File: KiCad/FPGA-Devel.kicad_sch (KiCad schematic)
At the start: 4 parts

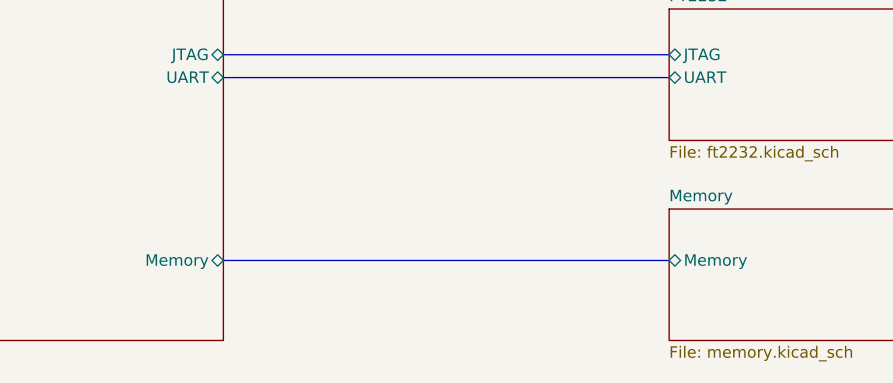
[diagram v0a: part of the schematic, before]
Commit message: micro-SD hinzugefügt
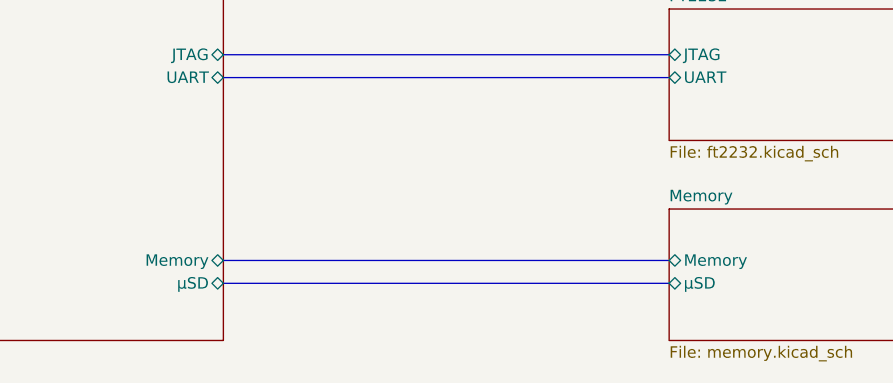
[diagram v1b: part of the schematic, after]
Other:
- sheet FPGA ports: added μSD; removed none
- sheet Memory ports: added μSD; removed none
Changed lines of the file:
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@@
+	(bus
+		(pts
+			(xy 152.4 152.4) (xy 201.93 152.4)
+		)
+		(stroke
+			(width 0)
+			(type default)
+		)
+	)
 	(bus
 		(pts
@@
 			)
 		)
+		(pin "μSD" bidirectional
+			(at 152.4 152.4 0)
+			(effects
+				(font
+					(size 1.27 1.27)
+				)
+				(justify right)
+			)
+		)
 		(instances
 			(project "FPGA-Devel"
@@
 			(effects
 				(font
+					(size 1.27 1.27)
+				)
+				(justify left)
+			)
+		)
+		(pin "μSD" bidirectional
+			(at 201.93 152.4 180)
+			(effects
+				(font
